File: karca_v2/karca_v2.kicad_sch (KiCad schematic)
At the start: 7 parts

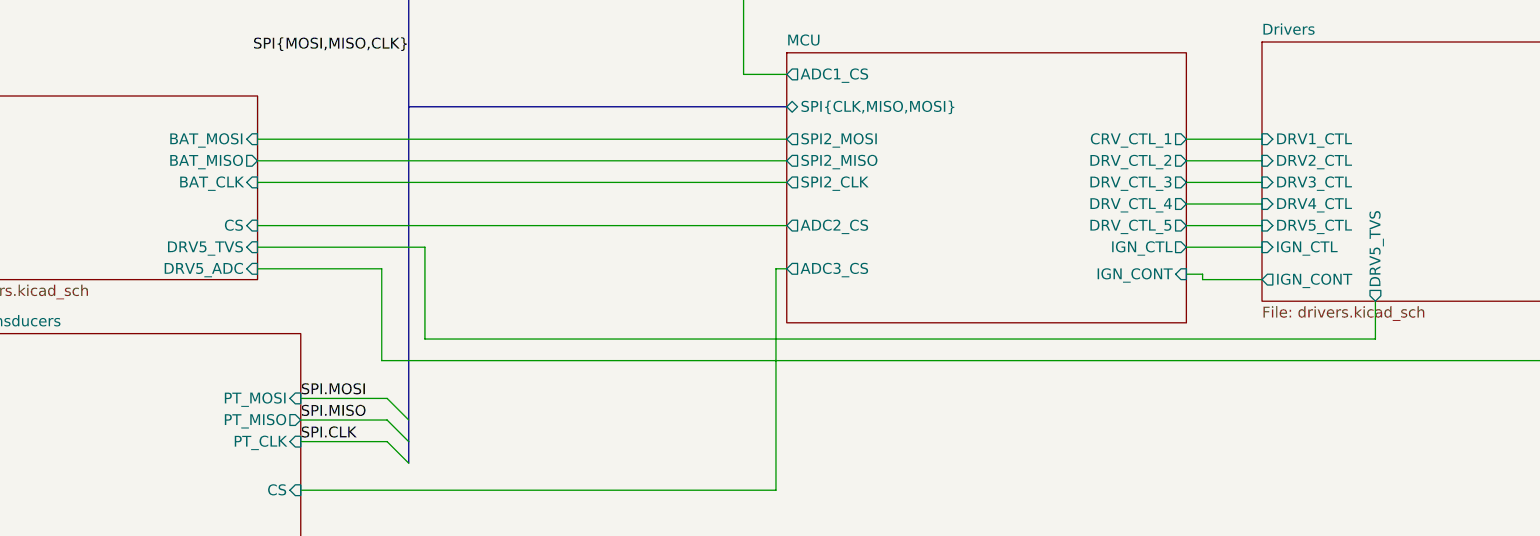
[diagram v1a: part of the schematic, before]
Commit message: fixed all routing. Now need to clean up vias
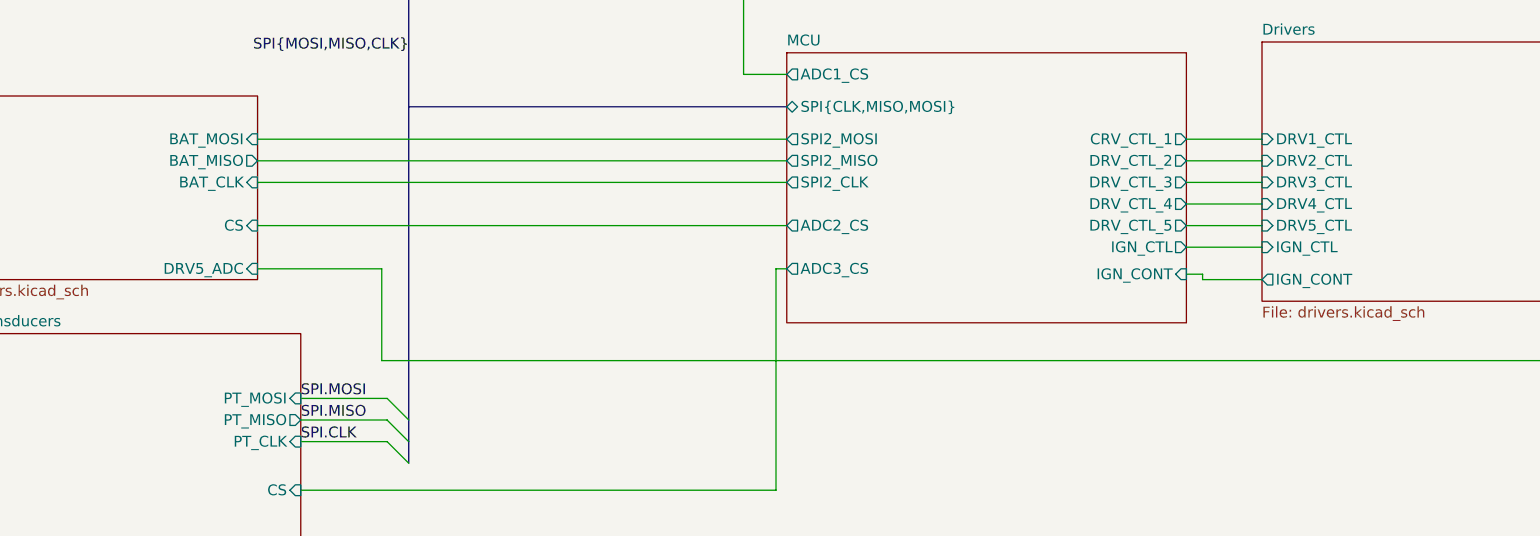
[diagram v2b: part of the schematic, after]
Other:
- sheet Drivers ports: added none; removed DRV5_TVS
- sheet Regulators ports: added none; removed DRV5_TVS
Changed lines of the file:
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@@
-	(wire
-		(pts
-			(xy 117.475 119.38) (xy 97.79 119.38)
-		)
-		(stroke
-			(width 0)
-			(type default)
-		)
-	)
 	(wire
 		(pts
@@
 	(wire
 		(pts
-			(xy 229.235 125.73) (xy 229.235 130.175)
-		)
-		(stroke
-			(width 0)
-			(type default)
-		)
-	)
-	(wire
-		(pts
 			(xy 175.26 69.85) (xy 187.96 69.85)
 		)
@@
 	(wire
 		(pts
-			(xy 229.235 130.175) (xy 117.475 130.175)
-		)
-		(stroke
-			(width 0)
-			(type default)
-		)
-	)
-	(wire
-		(pts
 			(xy 31.115 186.69) (xy 31.115 67.945)
 		)
@@
 		(pts
 			(xy 207.01 109.22) (xy 215.9 109.22)
-		)
-		(stroke
-			(width 0)
-			(type default)
-		)
-	)
-	(wire
-		(pts
-			(xy 117.475 130.175) (xy 117.475 119.38)
 		)
 		(stroke
@@
 			)
 		)
-		(pin "DRV5_TVS" output
-			(at 229.235 125.73 270)
-			(effects
-				(font
-					(size 1.27 1.27)
-				)
-				(justify left)
-			)
-		)
 		(pin "DRV1_ADC" output
 			(at 267.97 110.49 0)
@@
 			(effects
 				(font
-					(size 1.27 1.27)
-				)
-				(justify right)
-			)
-		)
-		(pin "DRV5_TVS" input
-			(at 97.79 119.38 0)
-			(effects
-				(font

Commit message: final production version
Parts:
- C13: MPN (none) -> C28323
- D4: MPN (none) -> C126807
- R2: MPN (none) -> C4177
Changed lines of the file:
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@@
+			)
+		)
+		(property "MPN" "C28323"
+			(at 175.26 62.23 90)
+			(effects
+				(font
+					(size 1.27 1.27)
+				)
+				(hide yes)
 			)
 		)
@@
 					(size 1.27 1.27)
 				)
+			)
+		)
+		(property "MPN" "C4177"
+			(at 187.96 50.8 0)
+			(effects
+				(font
+					(size 1.27 1.27)
+				)
+				(hide yes)
 			)
 		)
@@
 			(effects
 				(font
+					(size 1.27 1.27)
+				)
+				(hide yes)
+			)
+		)
+		(property "MPN" "C126807"
+			(at 187.96 64.77 90)
+			(effects
+				(font
